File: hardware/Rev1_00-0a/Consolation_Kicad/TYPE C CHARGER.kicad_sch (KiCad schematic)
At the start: 2 parts, among them J4 12401598E4#2A, U1 BQ25640VDLR

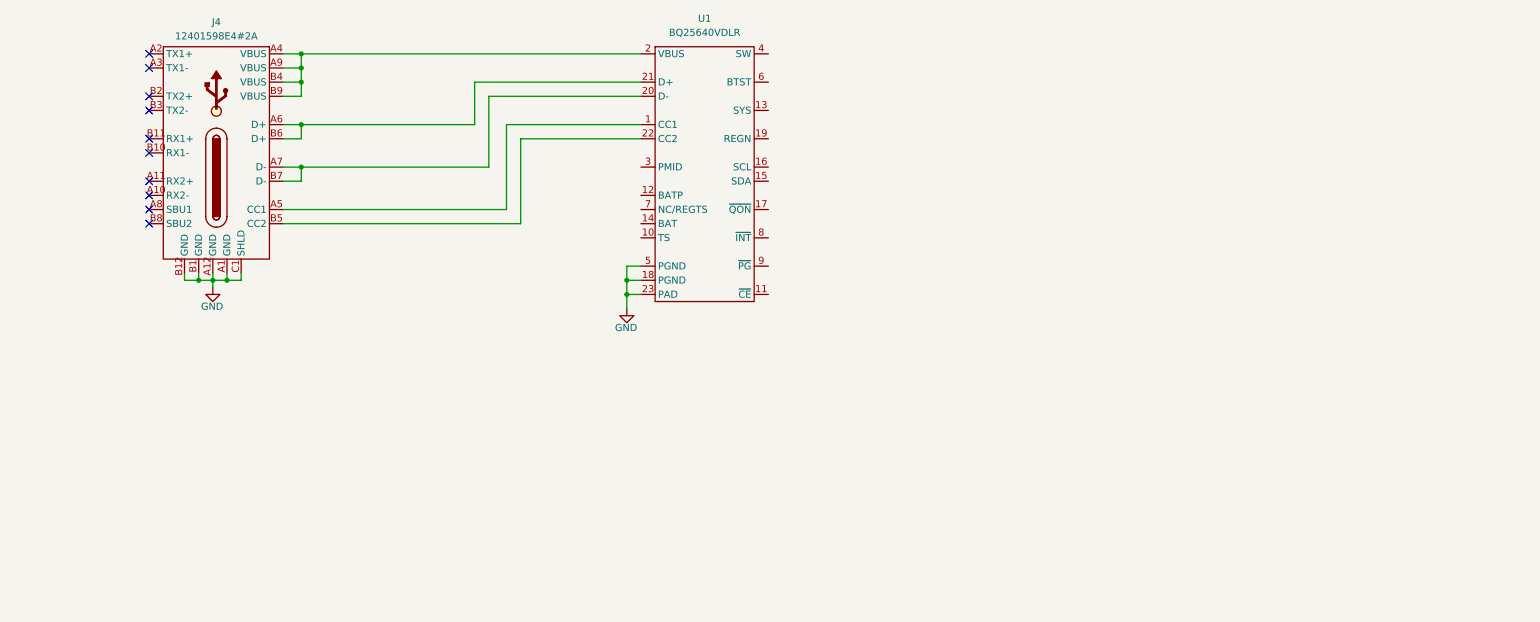
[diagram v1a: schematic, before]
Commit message: Update block diagram Updage charger schematic page with BQ25640 preliminary implementation
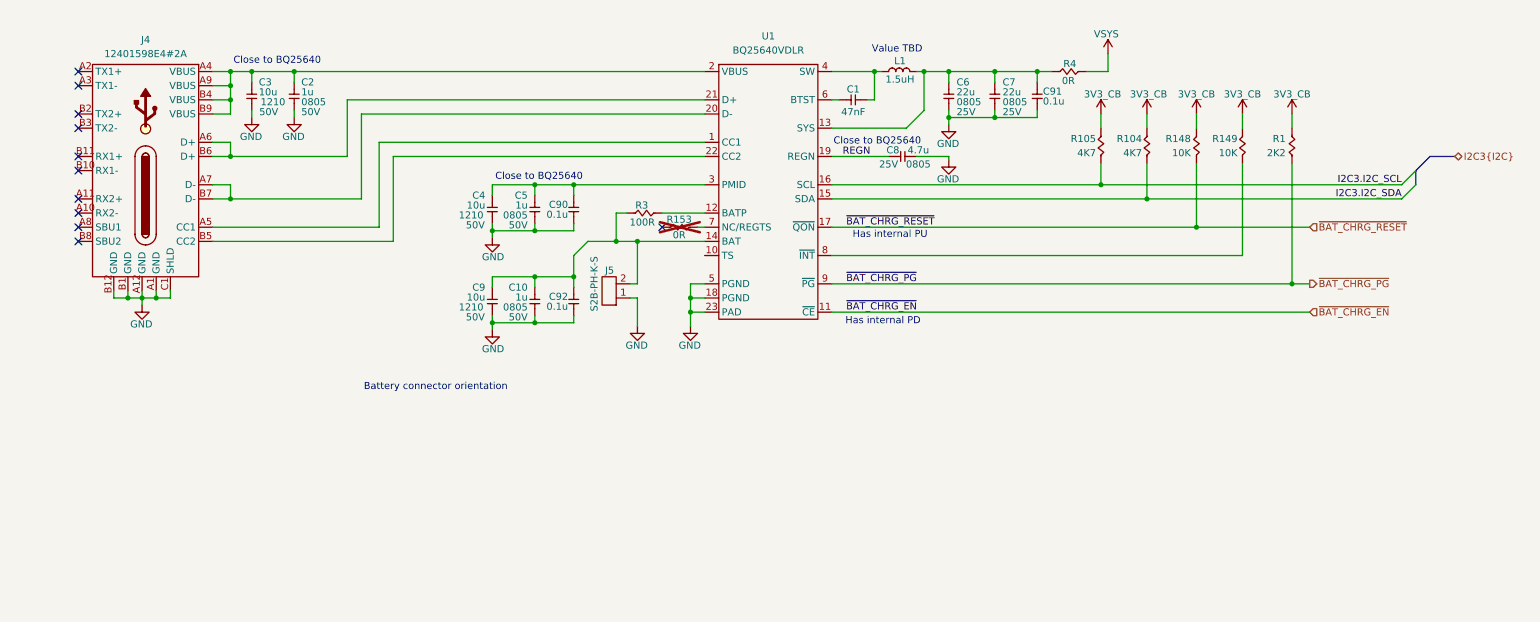
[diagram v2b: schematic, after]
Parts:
- added C1: 47nF, footprint:CAP_NONPOL_0402, symbol KicadCompDb:Capacitors/CAP_CER_SMT_00016
- added C10, C2, C5: 1u, footprint:CAP_NONPOL_0805, symbol KicadCompDb:Capacitors/CAP_CER_SMT_00002
- added C3, C4, C9: 10u, footprint:CAP_NONPOL_1210, symbol KicadCompDb:Capacitors/CAP_CER_SMT_00014
- added C6, C7: 22u, footprint:CAP_NONPOL_0805, symbol KicadCompDb:Capacitors/CAP_CER_SMT_00011
- added C8: 4.7u, footprint:CAP_NONPOL_0805, symbol KicadCompDb:Capacitors/CAP_CER_SMT_00017
- added C90, C91, C92: 0.1u, footprint:CAP_NONPOL_0402, symbol KicadCompDb:Capacitors/CAP_CER_SMT_00001
- added J5: S2B-PH-K-S, footprint:S2B-PH-K-S, symbol KicadCompDb:Connector/CONN_00025
- added L1: PA5003.152NLT, footprint:PA5003, symbol KicadCompDb:Inductor/IND_00009
- added R1: 2K2, footprint:RES_0402, symbol KicadCompDb:Resistors/RES_SMT_00008
- added R104, R105: 4K7, footprint:RES_0402, symbol KicadCompDb:Resistors/RES_SMT_00010
- added R148, R149: 10K, footprint:RES_0402, symbol KicadCompDb:Resistors/RES_SMT_00013
- added R153: 0R, footprint:RES_0402, symbol KicadCompDb:Resistors/RES_SMT_00001
- added R3: 100R, footprint:RES_0402, symbol KicadCompDb:Resistors/RES_SMT_00035
- added R4: 0R, footprint:RES_1206, symbol KicadCompDb:Resistors/RES_SMT_00022
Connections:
- net GND: now also C10.1, C2.1, C3.1, C4.1, C5.1, C6.1, C7.1, C8.2, C9.1, C90.1, C91.1, C92.1, J5.1
- net at J4.A4 (VBUS), J4.A9 (VBUS), J4.B4 (VBUS)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: now also C2.2, C3.2
- net ~{BAT_CHRG_EN}: now reaches U1.11 (~{CE})
- net at U1.12 (BATP): now also R3.2
- net at U1.13 (SYS): now also C6.2, C7.2, C91.2, L1.2, R4.1
- net at U1.14 (BAT): now also C10.2, C9.2, C92.2, J5.2, R3.1
- net I2C3.I2C_SDA: now reaches U1.15 (SDA)
- net I2C3.I2C_SDA: now also R104.1
- net I2C3.I2C_SCL: now reaches U1.16 (SCL)
- net I2C3.I2C_SCL: now also R105.1
- net ~{BAT_CHRG_RESET}: now reaches U1.17 (~{QON})
- net ~{BAT_CHRG_RESET}: now also R148.1
- net REGN: now reaches U1.19 (REGN)
- net REGN: now also C8.1
- net at U1.3 (PMID): now also C4.2, C5.2, C90.2
- net at U1.4 (SW): now also C1.1, L1.1
- net at U1.6 (BTST): now also C1.2
- net at U1.7 (NC/REGTS): now also R153.2
- net at U1.8 (~{INT}): now also R149.1
- net ~{BAT_CHRG_PG}: now reaches U1.9 (~{PG})
- net ~{BAT_CHRG_PG}: now also R1.1
- new net 3V3_CB: R1.2, R104.2, R105.2, R148.2, R149.2
- new net VSYS: R4.2
- no-connect marks 10 -> 11
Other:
- note added: "Battery connector orientation"
- note added: "Close to BQ25640"
- note added: "Has internal PD"
- note added: "Has internal PU"
- note added: "Value TBD"
- moved on the sheet: J4, U1

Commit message: Add part number of codec to block diagram Add codec and hdmi schematic sheets
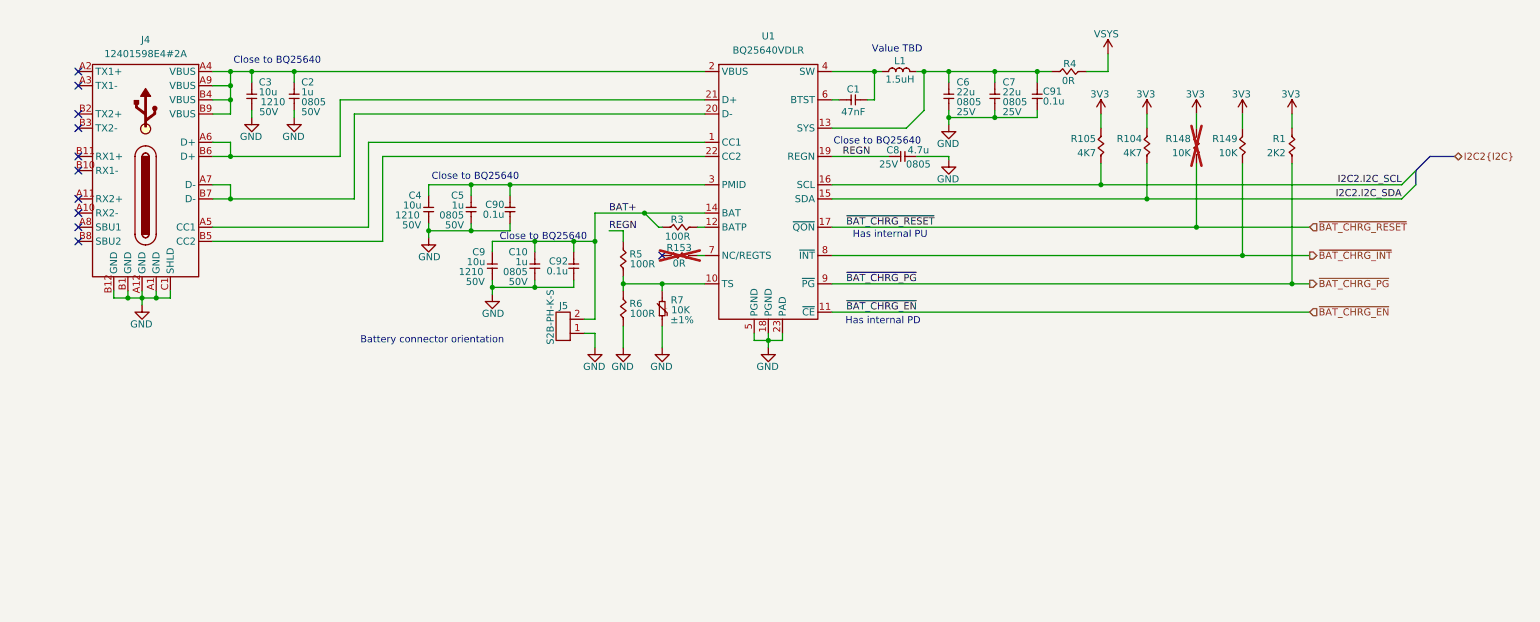
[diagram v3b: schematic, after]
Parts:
- added R5, R6: 100R, footprint:RES_0402, symbol KicadCompDb:Resistors/RES_SMT_00035
- added R7: 103AT-4-70374, footprint:HEADER_2P_2_54MM, symbol KicadCompDb:Miscellaneous/MIS_00013
- R148: now not fitted
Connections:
- net GND: now also R6.1, R7.1
- net REGN: now also R5.2
- net BAT+: now reaches C10.2, C9.2, C92.2, J5.2, R3.1, U1.14 (BAT)
- net ~{BAT_CHRG_INT}: now reaches R149.1, U1.8 (~{INT})
- net at U1.10 (TS): now also R5.1, R6.2, R7.2
- net 3V3_CB renamed 3V3
- net I2C3.I2C_SCL renamed I2C2.I2C_SCL
- net I2C3.I2C_SDA renamed I2C2.I2C_SDA
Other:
- moved on the sheet: C10, C4, C5, C9, C90, C92, J5, R153, R3

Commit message: Update schematics, block diagram and pin mux (good progress G)
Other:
- note added: "Resistors are 1% 1/16W 0402 unless otherwise noted Capacitors are 10% 50V X7R 0402 unless otherwise noted"
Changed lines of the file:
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@@
+		)
+	)
+	(text "Resistors are 1% 1/16W 0402 unless otherwise noted\nCapacitors are 10% 50V X7R 0402 unless otherwise noted"
+		(exclude_from_sim no)
+		(at 12.7 170.942 0)
+		(effects
+			(font
+				(size 1.27 1.27)
+			)
+			(justify left)
 		)
 	)

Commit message: Work on ConJoy [Consolation Joycon] Work on Consolation [Console Emulation]
- Adjust controller pinout
- Design controller for 1-PCB fits both side (reversible design for L-R controller)
- Preliminary PCB for 3d modeling
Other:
- note added: "Add ESD diodes"
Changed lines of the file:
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@@
 	(title_block
 		(title "Consolation [Console Emulation]")
-		(date "2026-07-09")
+		(date "2026-07-31")
 		(rev "1.00-0a")
 		(comment 1 "Jean-Francois Bilodeau")
@@
 			)
 		)
+	)
+	(text "Add ESD diodes"
+		(exclude_from_sim no)
+		(at 63.5 110.998 0)
+		(effects
+			(font
+				(size 2.54 2.54)
+				(color 194 0 0 1)
+			)
+		)

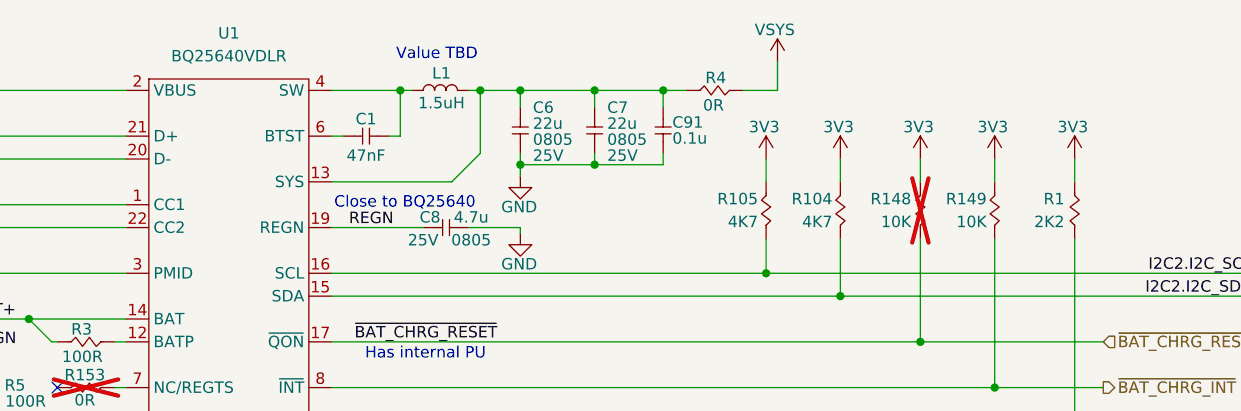
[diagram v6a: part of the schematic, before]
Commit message: Work on block diagram and top-level schematic sheet Work on PinMux
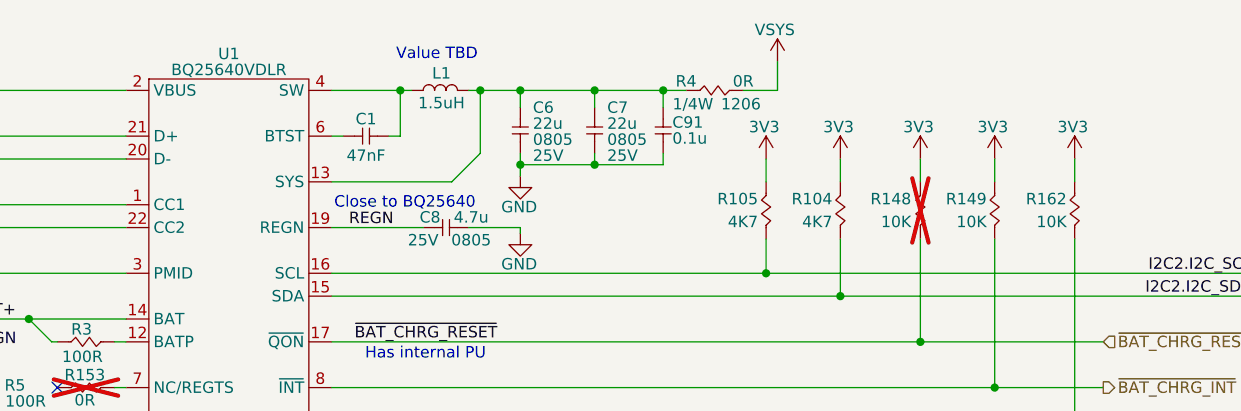
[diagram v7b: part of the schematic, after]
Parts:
- removed R1: 2K2, footprint:RES_0402, symbol KicadCompDb:Resistors/RES_SMT_00008
- added R162: 10K, footprint:RES_0402, symbol KicadCompDb:Resistors/RES_SMT_00013
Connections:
- net 3V3: now also R162.2
- net ~{BAT_CHRG_PG}: now also R162.1
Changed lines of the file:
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@@
 	)
 	(symbol
-		(lib_id "KicadCompDb:Resistors/RES_SMT_00008")
-		(at 242.57 91.44 90)
-		(unit 1)
-		(body_style 1)
-		(exclude_from_sim no)
-		(in_bom yes)
-		(on_board yes)
-		(in_pos_files yes)
-		(dnp no)
-		(property "Reference" "R1"
-			(at 241.427 88.265 90)
-			(show_name no)
-			(do_not_autoplace no)
-			(effects
-				(font
-					(size 1.27 1.27)
-				)
-				(justify left)
-			)
-		)
-		(property "Value" "2K2"
-			(at 241.427 90.805 90)
-			(show_name no)
-			(do_not_autoplace no)
-			(effects
-				(font
-					(size 1.27 1.27)
-				)
-				(justify left)
-			)
-		)
-		(property "Footprint" "footprint:RES_0402"
-			(at 264.668 90.932 0)
-			(hide yes)
-			(show_name no)
-			(do_not_autoplace no)
-			(effects
-				(font
-					(size 1.27 1.27)
-				)
-			)
-		)
-		(property "Datasheet" "https://www.yageogroup.com/content/datasheet/asset/file/PYU-RC_51_ROHS_P"
-			(at 242.57 91.44 0)
-			(hide yes)
-			(show_name no)
-			(do_not_autoplace no)
-			(effects
-				(font
-					(size 1.27 1.27)
-				)
-			)
-		)
-		(property "Description" "RES 2.2K OHM 1% 1/16W 0402"
-			(at 252.476 89.662 0)
-			(hide yes)
-			(show_name no)
-			(do_not_autoplace no)
-			(effects
-				(font
-					(size 1.27 1.27)
-				)
-			)
-		)
-		(property "Dimensions" "1.00mm x 0.50mm"
-			(at 242.57 91.44 0)
-			(hide yes)
-			(show_name yes)
-			(do_not_autoplace no)
-			(effects
-				(font
-					(size 1.27 1.27)
-				)
-			)
-		)
-		(property "Type" "RES SMT"
-			(at 242.57 91.44 0)
-			(hide yes)
-			(show_name yes)
-			(do_not_autoplace no)
-			(effects
-				(font
-					(size 1.27 1.27)
-				)
-			)
-		)
-		(property "Tolerance" "1%"
-			(at 262.89 91.186 0)
-			(hide yes)
-			(show_name no)
-			(do_not_autoplace no)
-			(effects
-				(font
-					(size 1.27 1.27)
-				)
-			)
-		)
-		(property "Power" "1/16W"
-			(at 256.794 91.186 0)
-			(hide yes)
-			(show_name no)
-			(do_not_autoplace no)
-			(effects
-				(font
-					(size 1.27 1.27)
-				)
-			)
-		)
-		(property "Package" "0402"
-			(at 258.826 91.44 0)
-			(hide yes)
-			(show_name no)
-			(do_not_autoplace no)
-			(effects
-				(font
-					(size 1.27 1.27)
-				)
-			)
-		)
-		(property "Manufacturer" "YAGEO"
-			(at 260.858 91.186 0)
-			(hide yes)
-			(show_name no)
-			(do_not_autoplace no)
-			(effects
-				(font
-					(size 1.27 1.27)
-				)
-			)
-		)
-		(property "Manufacturer Part Number" "RC0402FR-072K2P"
-			(at 250.444 91.186 0)
-			(hide yes)
-			(show_name no)
-			(do_not_autoplace no)
-			(effects
-				(font
-					(size 1.27 1.27)
-				)
-			)
-		)
-		(property "Distributor" "DigiKey"
-			(at 248.412 91.44 0)
-			(hide yes)
-			(show_name no)
-			(do_not_autoplace no)
-			(effects
-				(font
-					(size 1.27 1.27)
-				)
-			)
-		)
-		(property "Distributor Part Number" "YAG1260CT-ND"
-			(at 254.762 90.678 0)
-			(hide yes)
-			(show_name no)
-			(do_not_autoplace no)
-			(effects
-				(font
-					(size 1.27 1.27)
-				)
-			)
-		)
-		(property "Temperature Coefficient" "±100ppm/°C"
-			(at 242.57 91.44 0)
-			(hide yes)
-			(show_name no)
-			(do_not_autoplace no)
-			(effects
-				(font
-					(size 1.27 1.27)
-				)
-			)
-		)
-		(property "Operating Temperature" "-55°C ~ 155°C"
-			(at 266.954 90.678 0)
-			(hide yes)
-			(show_name no)
-			(do_not_autoplace no)
-			(effects
-				(font
-					(size 1.27 1.27)
-				)
-			)
-		)
-		(pin "1"
-		)
-		(pin "2"
-		)
-		(instances
-			(project "Consolation_Kicad"
-				(path "/b18b5a64-cfe0-4447-acaf-556f3c6e6513/e7d38f96-19c4-4995-a877-8c1df288247f"
-					(reference "R1")
-					(unit 1)
-				)
-			)
-		)
-	)
-	(symbol
 		(lib_id "KicadCompDb:Regulator/REG_00014")
 		(at 139.7 74.93 0)
@@
 		(in_pos_files yes)
 		(dnp no)
-		(fields_autoplaced yes)
 		(property "Reference" "U1"
-			(at 148.59 69.85 0)
+			(at 148.59 72.136 0)
 			(show_name no)
 			(do_not_autoplace no)
@@
 		)
 		(property "Value" "BQ25640VDLR"
-			(at 148.59 72.39 0)
+			(at 148.59 73.914 0)
 			(show_name no)
 			(do_not_autoplace no)
@@
 		(dnp no)
 		(property "Reference" "R4"
-			(at 202.692 74.803 0)
+			(at 199.39 75.184 0)
 			(show_name no)
 			(do_not_autoplace no)
@@
 		)
 		(property "Value" "0R"
-			(at 202.438 77.851 0)
+			(at 205.74 75.184 0)
 			(show_name no)
 			(do_not_autoplace no)
@@
 		)
 		(property "Power" "1/4W"
-			(at 202.565 73.025 0)
-			(hide yes)
+			(at 200.152 77.724 0)
 			(show_name no)
 			(do_not_autoplace no)
@@
 		)
 		(property "Package" "1206"
-			(at 200.66 92.456 0)
-			(hide yes)
+			(at 205.486 77.724 0)
 			(show_name no)
 			(do_not_autoplace no)
@@
 					(unit 1)
 				)
+			)
+		)
+	)
+	(symbol
+		(lib_id "KicadCompDb:Resistors/RES_SMT_00013")
+		(at 242.57 91.44 270)
+		(mirror x)
+		(unit 1)
+		(body_style 1)
+		(exclude_from_sim no)
+		(in_bom yes)
+		(on_board yes)
+		(in_pos_files yes)
+		(dnp no)
+		(property "Reference" "R162"
+			(at 241.681 88.265 90)
+			(show_name no)
+			(do_not_autoplace no)
+			(effects
+				(font
+					(size 1.27 1.27)
+				)
+				(justify right)
+			)
+		)
+		(property "Value" "10K"
+			(at 241.681 90.805 90)
+			(show_name no)
+			(do_not_autoplace no)
+			(effects
+				(font
+					(size 1.27 1.27)
+				)
+				(justify right)
+			)
+		)
+		(property "Footprint" "footprint:RES_0402"
+			(at 220.472 90.932 0)
+			(hide yes)
+			(show_name no)
+			(do_not_autoplace no)
+			(effects
+				(font
+					(size 1.27 1.27)
+				)
+			)
+		)
+		(property "Datasheet" "https://www.yageogroup.com/content/datasheet/asset/file/PYU-RC_GROUP_51_ROHS_L"
+			(at 242.57 91.44 0)
+			(hide yes)
+			(show_name no)
+			(do_not_autoplace no)
+			(effects
+				(font
+					(size 1.27 1.27)
+				)
+			)
+		)
+		(property "Description" "RES 10K OHM 1% 1/16W 0402"
+			(at 232.664 89.662 0)
+			(hide yes)
+			(show_name no)
+			(do_not_autoplace no)
+			(effects
+				(font
+					(size 1.27 1.27)
+				)
+			)
+		)
+		(property "Tolerance" "1%"
+			(at 222.25 91.186 0)
+			(hide yes)
+			(show_name no)
+			(do_not_autoplace no)
+			(effects
+				(font
+					(size 1.27 1.27)
+				)
+			)
+		)
+		(property "Power" "1/16W"
+			(at 228.346 91.186 0)
+			(hide yes)
+			(show_name no)
+			(do_not_autoplace no)
+			(effects
+				(font
+					(size 1.27 1.27)
+				)
+			)
+		)
+		(property "Package" "0402"
+			(at 226.314 91.44 0)
+			(hide yes)
+			(show_name no)
+			(do_not_autoplace no)
+			(effects
+				(font
+					(size 1.27 1.27)
+				)
+			)
+		)
+		(property "Manufacturer" "YAGEO"
+			(at 224.282 91.186 0)
+			(hide yes)
+			(show_name no)
+			(do_not_autoplace no)
+			(effects
+				(font
+					(size 1.27 1.27)
+				)
+			)
+		)
+		(property "Manufacturer Part Number" "RC0402FR-0710KL"
+			(at 234.696 91.186 0)
+			(hide yes)
+			(show_name no)
+			(do_not_autoplace no)
+			(effects
+				(font
+					(size 1.27 1.27)
+				)
+			)
+		)
+		(property "Distributor" "DigiKey"
+			(at 236.728 91.44 0)
+			(hide yes)
+			(show_name no)
+			(do_not_autoplace no)
+			(effects
+				(font
+					(size 1.27 1.27)
+				)
+			)
+		)
+		(property "Distributor Part Number" "311-10.0KLRCT-ND"
+			(at 230.378 90.678 0)
+			(hide yes)
+			(show_name no)
+			(do_not_autoplace no)
+			(effects
+				(font
+					(size 1.27 1.27)
+				)
+			)
+		)
+		(property "Temperature Coefficient" "±100ppm/°C"
+			(at 242.57 91.44 0)
+			(hide yes)
+			(show_name no)
+			(do_not_autoplace no)
+			(effects
+				(font
+					(size 1.27 1.27)
+				)
+			)
+		)
+		(property "Operating Temperature" "-55°C ~ 155°C"
+			(at 218.186 90.678 0)
+			(hide yes)
+			(show_name no)
+			(do_not_autoplace no)
+			(effects
+				(font
+					(size 1.27 1.27)
+				)
+			)
+		)
+		(property "Type" "RES SMT"
+			(at 242.57 91.44 0)
+			(hide yes)
+			(show_name yes)
+			(do_not_autoplace no)
+			(effects
+				(font
+					(size 1.27 1.27)
+				)
+			)
+		)
+		(property "Dimensions" "1.00mm x 0.50mm"
+			(at 242.57 91.44 0)
+			(hide yes)
+			(show_name yes)
+			(do_not_autoplace no)
+			(effects
+				(font
+					(size 1.27 1.27)
+				)
+			)
+		)
+		(pin "2"
+		)
+		(pin "1"
+		)
+		(instances
+			(project "Consolation_Kicad"
+				(path "/b18b5a64-cfe0-4447-acaf-556f3c6e6513/e7d38f96-19c4-4995-a877-8c1df288247f"
+					(reference "R162")
+					(unit 1)
+				)
